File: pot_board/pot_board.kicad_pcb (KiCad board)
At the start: 2 copper layers, 43.4 x 37 mm, 3 parts, among them J1 Conn_01x06

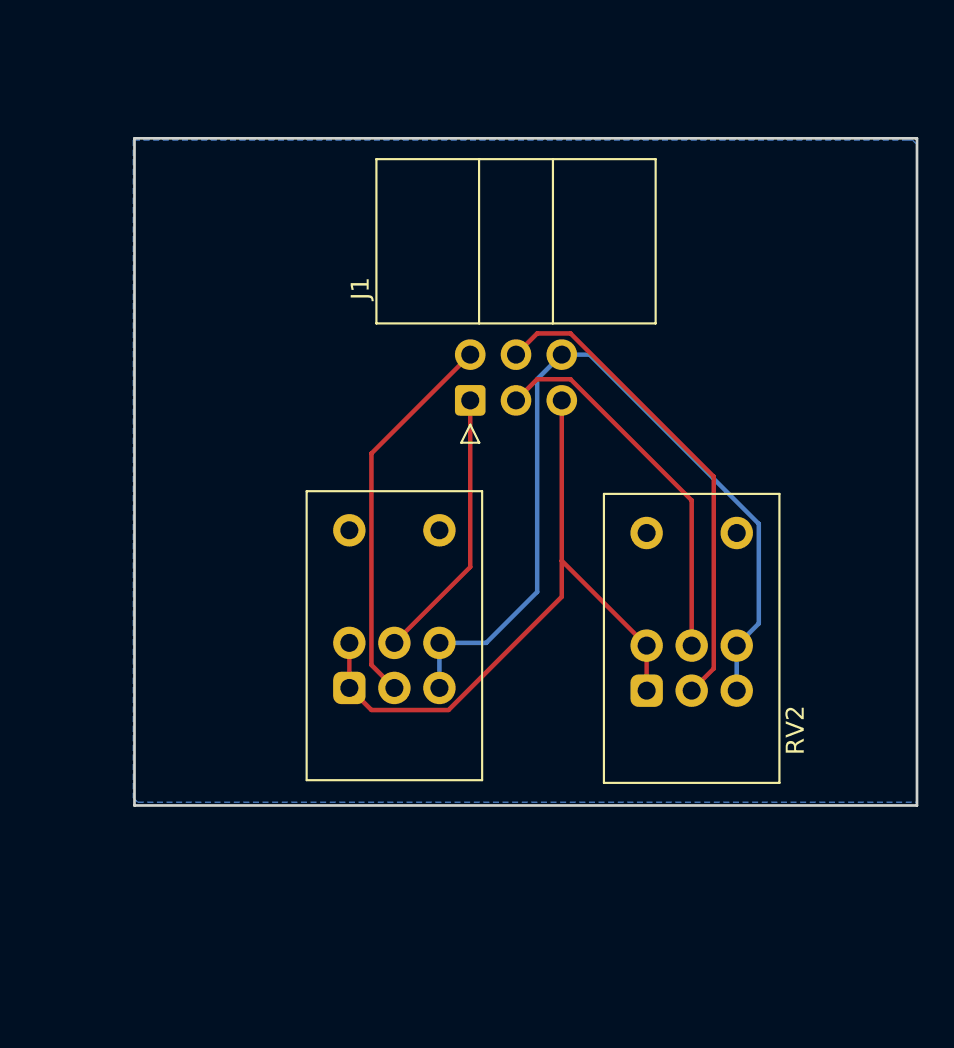
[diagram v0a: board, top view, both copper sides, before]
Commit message: update main board routing, add 3d models and improve layout
Changes:

* update main board layout a bit
* try to improve routing
* add 3d model for 6p6c
* add decoupling caps to ptt line
* almost finish pot board
* switch board almost finished

Details:
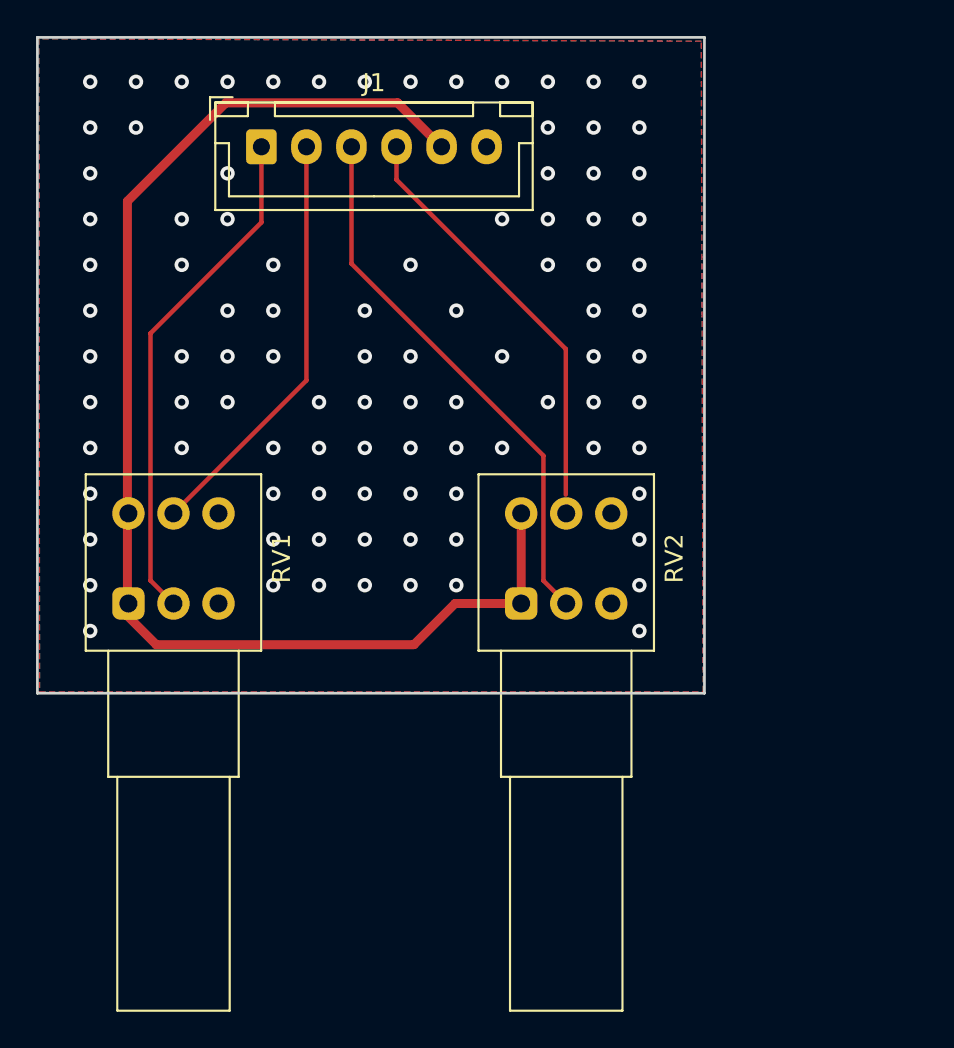
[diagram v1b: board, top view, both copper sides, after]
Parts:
- J1: footprint Connector_IDC:IDC-Header_2x03_P2.54mm_Horizontal -> Connector_JST:JST_XH_B6B-XH-A_1x06_P2.50mm_Vertical
- RV1, RV2: footprint Potentiometer_THT:Potentiometer_Alps_RK097_Dual_Horizontal_Switch -> CustomLibrary:Potentiometer_Alps_RK097_Dual_Horizontal
- moved J1 18.2 mm to (30.9, 19.4), turned to 0 degrees
- moved RV1 14.2 mm to (23.5, 42.2)
- moved RV2 10.1 mm to (45.3, 42.2)
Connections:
- RV1 pad 2: Net-(J1-Pin_2) -> Net-(J1-Pin_1)
- RV1 pad 5: Net-(J1-Pin_1) -> Net-(J1-Pin_2)
- RV2 pad 2: Net-(J1-Pin_4) -> Net-(J1-Pin_3)
- RV2 pad 5: Net-(J1-Pin_3) -> Net-(J1-Pin_4)
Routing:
- net GND: track 47.4 -> 0.00 mm, vias 0 -> 96
- net +3.3V: track 37.7 -> 72.2 mm
- net Net-(J1-Pin_1): track 15.2 -> 28.4 mm
- net Net-(J1-Pin_3): track 21.1 -> 30.3 mm
- net Net-(J1-Pin_4): track 27.1 -> 23.2 mm
- net Net-(J1-Pin_2): track 21.3 -> 23.4 mm
- added copper zone on F.Cu, net GND
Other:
- board size 43.4 x 37 mm -> 37 x 36.4 mm
- board text added: "Lenght from housing to shaft end"
- board text added: "Total length"
